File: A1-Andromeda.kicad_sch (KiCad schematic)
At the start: 39 parts, among them J1 Conn_01x02, J2 Conn_01x02, J3 Conn_01x02, J5 Conn_01x10_Pin, J6 Conn_01x10_Pin, J8 Conn_01x10_Pin, SW1 SW_SPST, SW2 SW_DIP_x02, U1 LM2940IMPX-5.0/NOPB, U2 NUCLEO-F042K6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

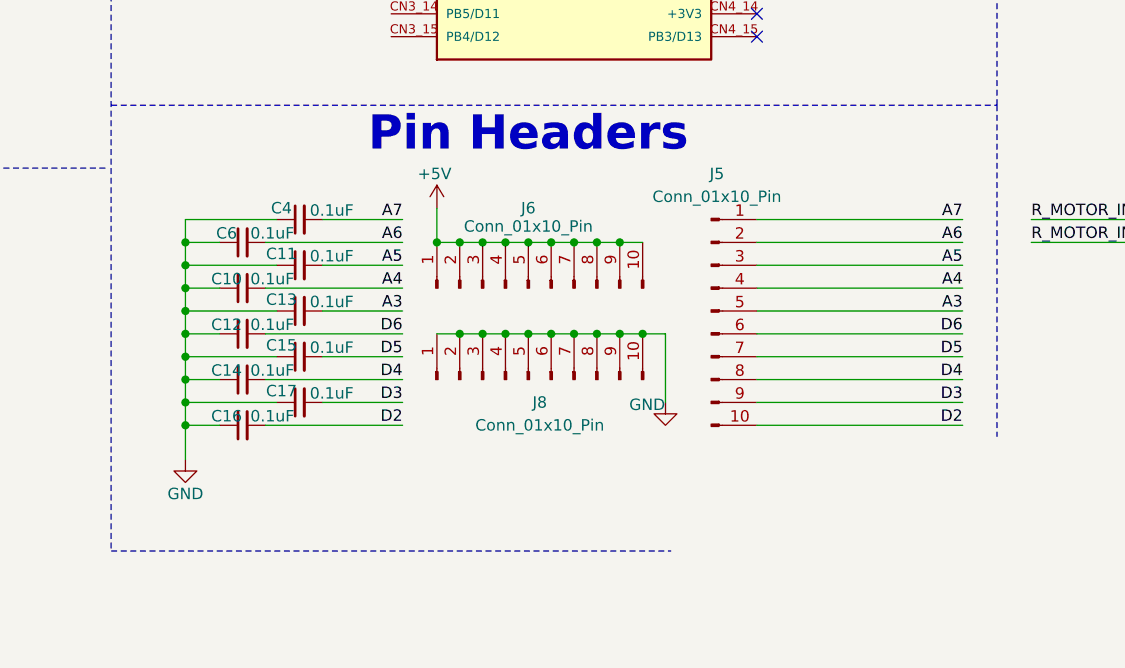
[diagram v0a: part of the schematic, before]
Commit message: remove bypass capacitors
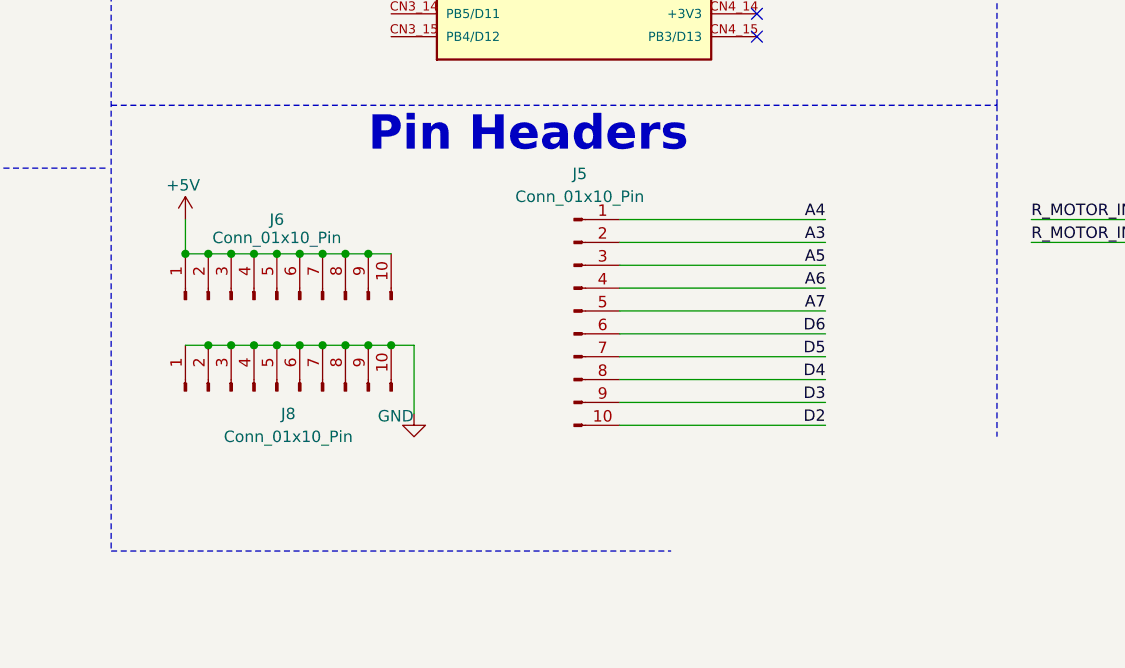
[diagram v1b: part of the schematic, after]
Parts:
- removed C10, C11, C12, C13, C14, C15, C16, C17, C4, C6: 0.1uF, Capacitor_SMD:C_1206_3216Metric, symbol Device:C_Small
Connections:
- net A3: now also J5.2 (Pin_2); no longer J5.5 (Pin_5)
- net A4: now also J5.1 (Pin_1); no longer J5.4 (Pin_4)
- net A6: now also J5.4 (Pin_4); no longer J5.2 (Pin_2)
- net A7: now also J5.5 (Pin_5); no longer J5.1 (Pin_1)
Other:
- moved on the sheet: J5, J6, J8

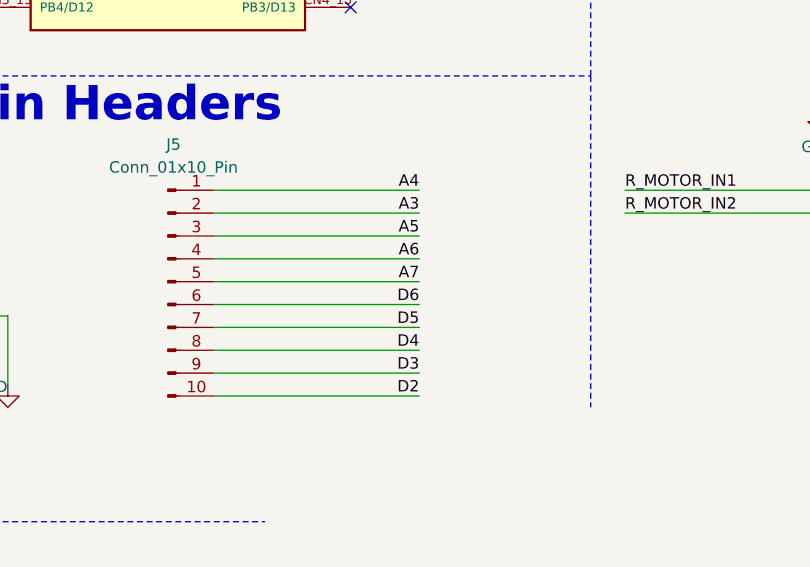
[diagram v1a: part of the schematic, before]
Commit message: rotate GPIO pin array
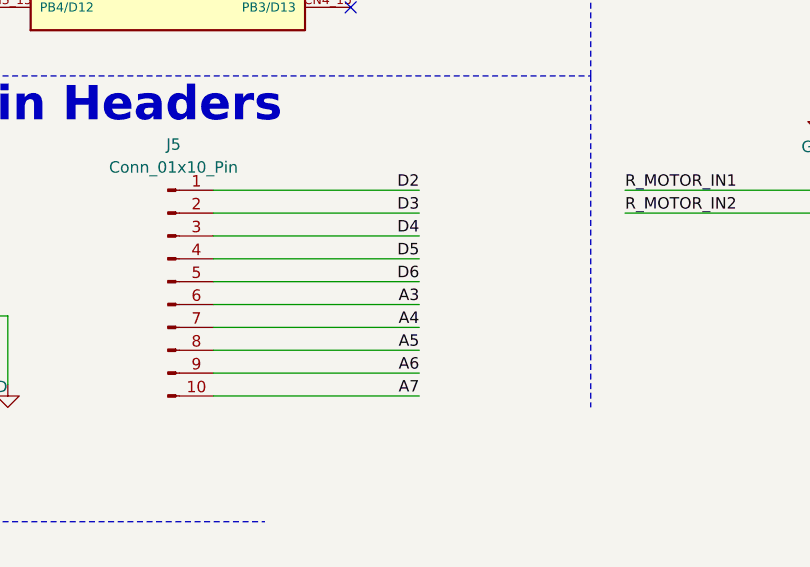
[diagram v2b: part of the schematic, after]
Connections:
- net A3: now also J5.6 (Pin_6); no longer J5.2 (Pin_2)
- net A4: now also J5.7 (Pin_7); no longer J5.1 (Pin_1)
- net A5: now also J5.8 (Pin_8); no longer J5.3 (Pin_3)
- net A6: now also J5.9 (Pin_9); no longer J5.4 (Pin_4)
- net A7: now also J5.10 (Pin_10); no longer J5.5 (Pin_5)
- net D2: now also J5.1 (Pin_1); no longer J5.10 (Pin_10)
- net D3: now also J5.2 (Pin_2); no longer J5.9 (Pin_9)
- net D4: now also J5.3 (Pin_3); no longer J5.8 (Pin_8)
- net D5: now also J5.4 (Pin_4); no longer J5.7 (Pin_7)
- net D6: now also J5.5 (Pin_5); no longer J5.6 (Pin_6)
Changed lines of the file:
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@@
+		)
+	)
+	(label "D6"
+		(at 194.31 152.4 180)
+		(effects
+			(font
+				(size 1.27 1.27)
+			)
+			(justify right bottom)
 		)
 	)
@@
 		)
 	)
-	(label "A5"
-		(at 194.31 147.32 180)
-		(effects
-			(font
-				(size 1.27 1.27)
-			)
-			(justify right bottom)
-		)
-	)
 	(label "D6"
 		(at 123.19 106.68 0)
@@
 		)
 	)
-	(label "D6"
+	(label "A4"
+		(at 194.31 157.48 180)
+		(effects
+			(font
+				(size 1.27 1.27)
+			)
+			(justify right bottom)
+		)
+	)
+	(label "D3"
+		(at 194.31 144.78 180)
+		(effects
+			(font
+				(size 1.27 1.27)
+			)
+			(justify right bottom)
+		)
+	)
+	(label "A3"
 		(at 194.31 154.94 180)
-		(effects
-			(font
-				(size 1.27 1.27)
-			)
-			(justify right bottom)
-		)
-	)
-	(label "A4"
-		(at 194.31 142.24 180)
-		(effects
-			(font
-				(size 1.27 1.27)
-			)
-			(justify right bottom)
-		)
-	)
-	(label "D4"
-		(at 194.31 160.02 180)
 		(effects
 			(font
@@
 		)
 	)
-	(label "A3"
-		(at 194.31 144.78 180)
-		(effects
-			(font
-				(size 1.27 1.27)
-			)
-			(justify right bottom)
-		)
-	)
 	(label "DIP_SWITCH_OUT2"
 		(at 186.69 44.45 180)
@@
 		)
 	)
+	(label "A6"
+		(at 194.31 162.56 180)
+		(effects
+			(font
+				(size 1.27 1.27)
+			)
+			(justify right bottom)
+		)
+	)
 	(label "A5"
 		(at 204.47 101.6 180)
@@
 		)
 	)
+	(label "D4"
+		(at 194.31 147.32 180)
+		(effects
+			(font
+				(size 1.27 1.27)
+			)
+			(justify right bottom)
+		)
+	)
 	(label "L_MOTOR_IN2"
 		(at 217.17 92.71 0)
@@
 		)
 	)
-	(label "A7"
-		(at 194.31 152.4 180)
-		(effects
-			(font
-				(size 1.27 1.27)
-			)
-			(justify right bottom)
-		)
-	)
-	(label "A6"
-		(at 194.31 149.86 180)
-		(effects
-			(font
-				(size 1.27 1.27)
-			)
-			(justify right bottom)
-		)
-	)
 	(label "A4"
 		(at 204.47 104.14 180)
@@
 		)
 	)
+	(label "D5"
+		(at 194.31 149.86 180)
+		(effects
+			(font
+				(size 1.27 1.27)
+			)
+			(justify right bottom)
+		)
+	)
+	(label "A5"
+		(at 194.31 160.02 180)
+		(effects
+			(font
+				(size 1.27 1.27)
+			)
+			(justify right bottom)
+		)
+	)
 	(label "D2"
-		(at 194.31 165.1 180)
+		(at 194.31 142.24 180)
 		(effects
 			(font
@@
 		)
 	)
-	(label "D5"
-		(at 194.31 157.48 180)
-		(effects
-			(font
-				(size 1.27 1.27)
-			)
-			(justify right bottom)
-		)
-	)
 	(label "DIP_SWITCH_OUT2"
 		(at 123.19 111.76 0)
@@
 		)
 	)
-	(label "D3"
-		(at 194.31 162.56 180)
-		(effects
-			(font
-				(size 1.27 1.27)
-			)
-			(justify right bottom)
-		)
-	)
 	(label "D2"
 		(at 123.19 96.52 0)
@@
 		)
 	)
+	(label "A7"
+		(at 194.31 165.1 180)
+		(effects
+			(font
+				(size 1.27 1.27)
+			)
+			(justify right bottom)
+		)
+	)

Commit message: redo PCB
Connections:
- net D2: now also J5.5 (Pin_5); no longer J5.1 (Pin_1)
- net D3: now also J5.4 (Pin_4); no longer J5.2 (Pin_2)
- net D5: now also J5.2 (Pin_2); no longer J5.4 (Pin_4)
- net D6: now also J5.1 (Pin_1); no longer J5.5 (Pin_5)
- no-connect marks 10 -> 12

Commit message: finish up
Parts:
- removed U2: NUCLEO-F042K6, footprints:MODULE_NUCLEO-F042K6, symbol NUCLEO-F042K6:NUCLEO-F042K6
- added D1: GREEN, LED_SMD:LED_1206_3216Metric, symbol Device:LED
- added J4: Conn_01x03_Socket, Connector_PinSocket_2.54mm:PinSocket_1x03_P2.54mm_Vertical, symbol Connector:Conn_01x03_Socket
- added R3, R4: 100K, Capacitor_SMD:C_1206_3216Metric, symbol Device:R_Small_US
- added R5: 220, Resistor_SMD:R_1206_3216Metric, symbol Device:R_Small_US
- added U5: NUCLEO-F042K6, NUCLEO-F042K6:MODULE_NUCLEO-F042K6, symbol NUCLEO-F042K6:NUCLEO-F042K6
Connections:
- net +5V: now also J4.3 (Pin_3), U5.CN4_4 (+5V)
- net A3: now also U5.CN4_9 (PA4/A3)
- net A4: now also U5.CN4_8 (PA5/A4)
- net A5: now also U5.CN4_7 (PA6/A5)
- net A6: now also U5.CN4_6 (PA7/A6)
- net A7: now also U5.CN4_5 (PA2/A7)
- net D2: now also U5.CN3_5 (PA12/D2)
- net D3: now also U5.CN3_6 (PB0/D3)
- net D4: now also U5.CN3_7 (PB7/D4)
- net D5: now also U5.CN3_8 (PB6/D5)
- net D6: now also U5.CN3_9 (PB1/D6)
- net DIP_SWITCH_OUT1: now also R4.1, U5.CN3_10 (PF0/D7)
- net DIP_SWITCH_OUT2: now also R3.1, U5.CN3_11 (PF1/D8)
- net GND: now also D1.1 (K), J4.1 (Pin_1), R3.2, R4.2, U5.CN3_4 (GND_CN3)
- net L_MOTOR_IN1: now also U5.CN3_13 (PA11/D10)
- net L_MOTOR_IN2: now also U5.CN3_12 (PA8/D9)
- net R_MOTOR_IN1: now also U5.CN3_2 (PA10/D0)
- net R_MOTOR_IN2: now also U5.CN3_1 (PA9/D1)
- net at F1.1, SW1.2 (B): now also R5.1
- new net: D1.2 (A), R5.2
- new net SRT_STP_MODULE: J4.2 (Pin_2), U5.CN3_14 (PB5/D11)
- no-connect marks 12 -> 11
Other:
- note added: "5V LDO"
- note added: "Input"
- note removed: "5V Buck Converter"
- note removed: "INPUT"
- moved on the sheet: J6, J8, SW1, SW2

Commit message: fix VIN
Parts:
- U5: footprint NUCLEO-F042K6:MODULE_NUCLEO-F042K6 -> footprints:MODULE_NUCLEO-F042K6
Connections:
- net +5V: now also U5.CN4_1 (VIN)
- no-connect marks 11 -> 10
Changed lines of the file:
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@@
 	)
 	(junction
+		(at 194.31 86.36)
+		(diameter 0)
+		(color 0 0 0 0)
+	)
+	(junction
 		(at 248.92 72.39)
 		(diameter 0)
@@
 	)
 	(no_connect
-		(at 186.69 86.36)
-	)
-	(no_connect
 		(at 186.69 111.76)
 	)
@@
 	(wire
 		(pts
+			(xy 194.31 78.74) (xy 194.31 86.36)
+		)
+		(stroke
+			(width 0)
+			(type default)
+		)
+	)
+	(wire
+		(pts
 			(xy 123.19 86.36) (xy 146.05 86.36)
 		)
@@
 	(wire
 		(pts
-			(xy 127 149.86) (xy 129.54 149.86)
+			(xy 194.31 86.36) (xy 194.31 93.98)
 		)
 		(stroke
@@
 	(wire
 		(pts
-			(xy 194.31 93.98) (xy 194.31 83.82)
+			(xy 127 149.86) (xy 129.54 149.86)
 		)
 		(stroke
@@
 	(wire
 		(pts
+			(xy 186.69 86.36) (xy 194.31 86.36)
+		)
+		(stroke
+			(width 0)
+			(type default)
+		)
+	)
+	(wire
+		(pts
 			(xy 46.99 93.98) (xy 44.45 93.98)
 		)
@@
 			)
 		)
-		(property "Footprint" "NUCLEO-F042K6:MODULE_NUCLEO-F042K6"
+		(property "Footprint" "footprints:MODULE_NUCLEO-F042K6"
 			(at 166.37 104.14 0)
 			(effects
@@
 	(symbol
 		(lib_id "power:+5P")
-		(at 194.31 83.82 0)
+		(at 194.31 78.74 0)
 		(unit 1)
 		(exclude_from_sim no)
@@
 		(dnp no)
 		(property "Reference" "#PWR09"
-			(at 194.31 87.63 0)
+			(at 194.31 82.55 0)
 			(effects
 				(font
@@
 		)
 		(property "Value" "+5V"
-			(at 194.31 80.264 0)
+			(at 194.31 75.184 0)
 			(effects
 				(font
@@
 		)
 		(property "Footprint" ""
-			(at 194.31 83.82 0)
+			(at 194.31 78.74 0)
 			(effects
 				(font
@@
 		)
 		(property "Datasheet" ""
-			(at 194.31 83.82 0)
+			(at 194.31 78.74 0)
 			(effects
 				(font
@@
 		)
 		(property "Description" "Power symbol creates a global label with name \"+5P\""
-			(at 194.31 83.82 0)
+			(at 194.31 78.74 0)
 			(effects
 				(font

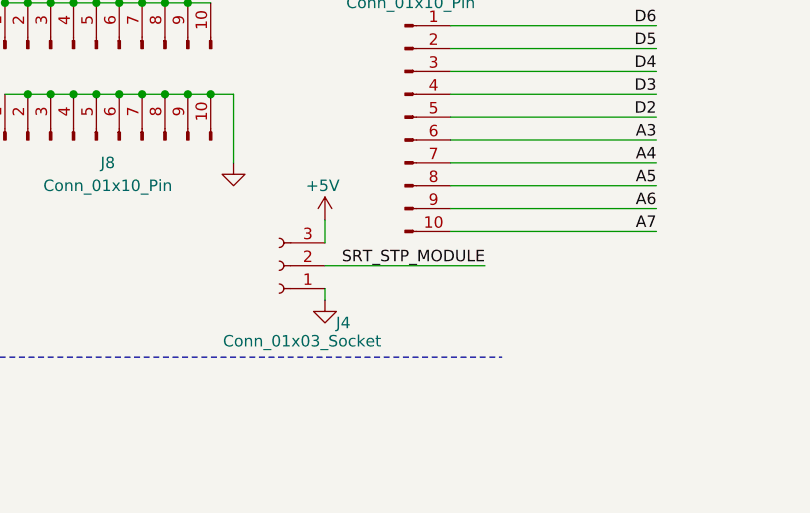
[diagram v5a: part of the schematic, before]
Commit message: fix start/stop module pins
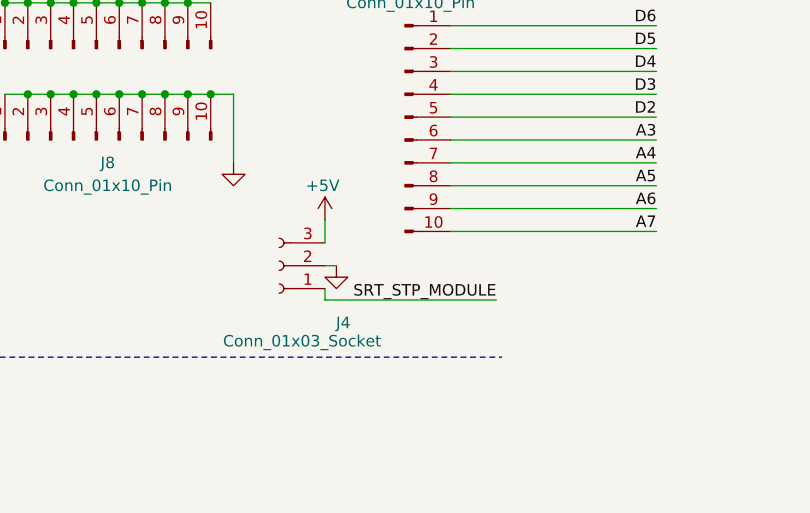
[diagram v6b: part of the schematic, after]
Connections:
- net GND: now also J4.2 (Pin_2); no longer J4.1 (Pin_1)
- net SRT_STP_MODULE: now also J4.1 (Pin_1); no longer J4.2 (Pin_2)
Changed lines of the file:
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@@
 	(wire
 		(pts
+			(xy 157.48 172.72) (xy 157.48 171.45)
+		)
+		(stroke
+			(width 0)
+			(type default)
+		)
+	)
+	(wire
+		(pts
 			(xy 124.46 149.86) (xy 127 149.86)
 		)
@@
 	(wire
 		(pts
-			(xy 175.26 168.91) (xy 157.48 168.91)
+			(xy 158.75 168.91) (xy 157.48 168.91)
 		)
 		(stroke
@@
 	(wire
 		(pts
-			(xy 157.48 172.72) (xy 157.48 171.45)
-		)
-		(stroke
-			(width 0)
-			(type default)
-		)
-	)
-	(wire
-		(pts
 			(xy 248.92 120.65) (xy 248.92 124.46)
 		)
@@
 	(wire
 		(pts
+			(xy 176.53 172.72) (xy 157.48 172.72)
+		)
+		(stroke
+			(width 0)
+			(type default)
+		)
+	)
+	(wire
+		(pts
 			(xy 238.76 78.74) (xy 241.3 78.74)
 		)
@@
 		)
 	)
-	(label "SRT_STP_MODULE"
-		(at 175.26 168.91 180)
+	(label "A3"
+		(at 204.47 106.68 180)
 		(effects
 			(font
@@
 		)
 	)
-	(label "A3"
-		(at 204.47 106.68 180)
+	(label "L_MOTOR_IN1"
+		(at 123.19 116.84 0)
 		(effects
 			(font
 				(size 1.27 1.27)
 			)
-			(justify right bottom)
+			(justify left bottom)
 		)
 	)
-	(label "L_MOTOR_IN1"
-		(at 123.19 116.84 0)
+	(label "SRT_STP_MODULE"
+		(at 176.53 172.72 180)
 		(effects
 			(font
 				(size 1.27 1.27)
 			)
-			(justify left bottom)
+			(justify right bottom)
 		)
 	)
@@
 	(symbol
 		(lib_id "power:GND")
-		(at 157.48 172.72 0)
+		(at 158.75 168.91 0)
 		(unit 1)
 		(exclude_from_sim no)
@@
 		(dnp no)
 		(property "Reference" "#PWR022"
-			(at 157.48 179.07 0)
+			(at 158.75 175.26 0)
 			(effects
 				(font
@@
 		)
 		(property "Value" "GND"
-			(at 155.448 172.974 0)
+			(at 156.718 169.164 0)
 			(effects
 				(font
@@
 		)
 		(property "Footprint" ""
-			(at 157.48 172.72 0)
+			(at 158.75 168.91 0)
 			(effects
 				(font
@@
 		)
 		(property "Datasheet" ""
-			(at 157.48 172.72 0)
+			(at 158.75 168.91 0)
 			(effects
 				(font
@@
 		)
 		(property "Description" "Power symbol creates a global label with name \"GND\" , ground"
-			(at 157.48 172.72 0)
+			(at 158.75 168.91 0)
 			(effects
 				(font
